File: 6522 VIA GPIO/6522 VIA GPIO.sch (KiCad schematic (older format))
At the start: 11 parts

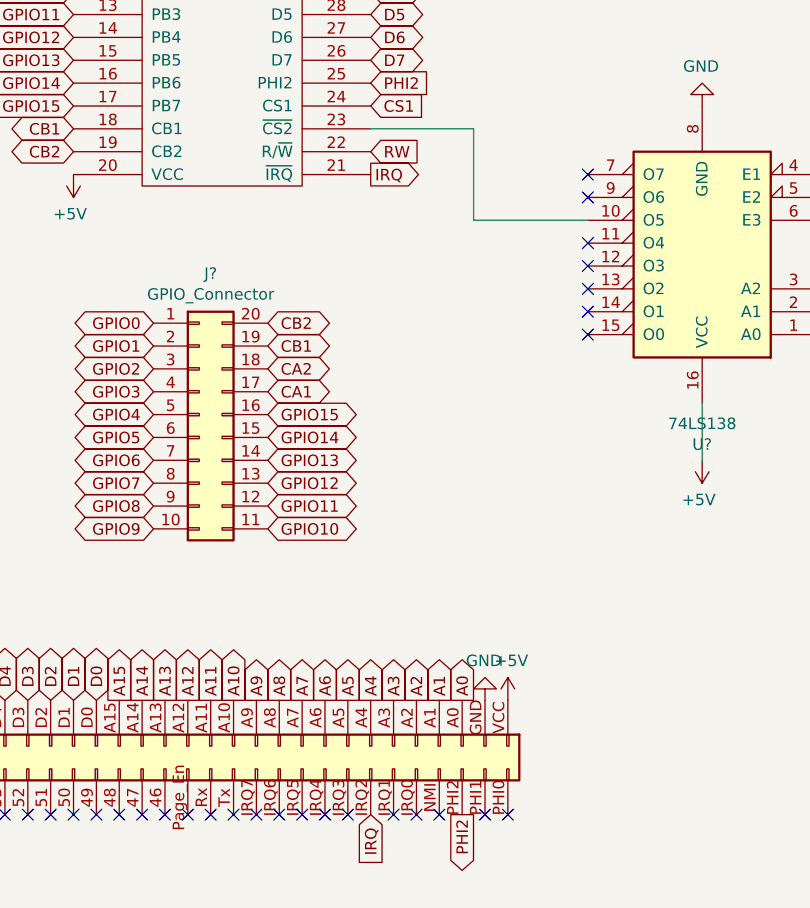
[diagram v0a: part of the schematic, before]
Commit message: Restored SerialIO back to 6521 PIA...
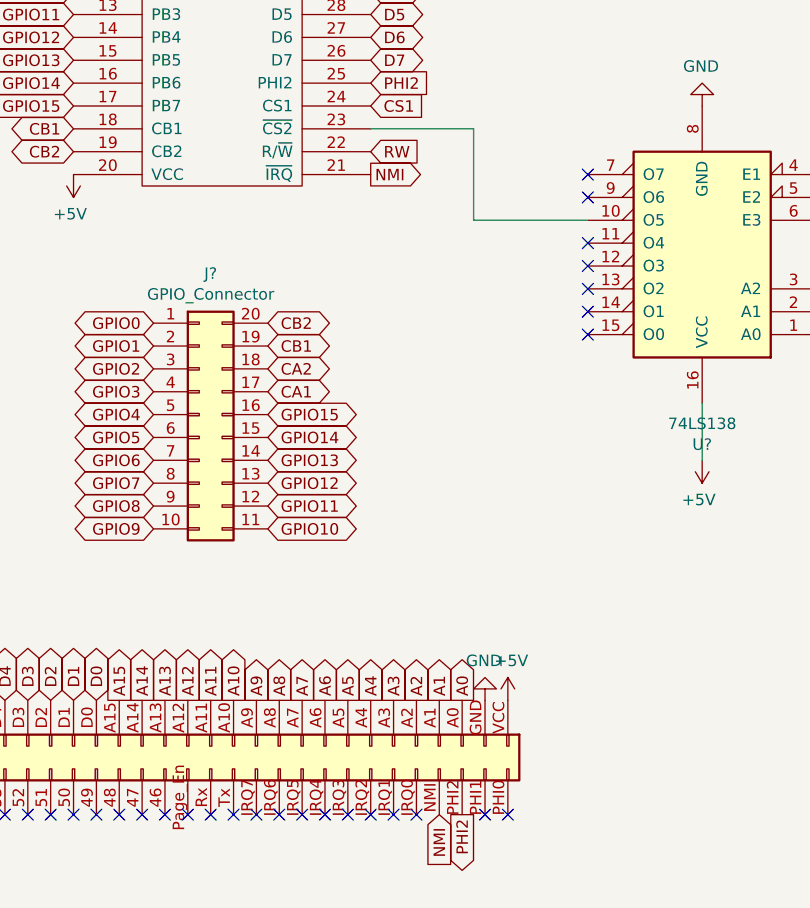
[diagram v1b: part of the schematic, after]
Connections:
- net NMI: now reaches J?.NMI
- net NMI: now also U?.21 (~IRQ)
- net IRQ: no longer names the net of J?.IRQ2
- net IRQ: no longer U?.21 (~IRQ)
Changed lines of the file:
@@
 Text GLabel 4450 3550 2    50   BiDi ~ 0
 D7
-Text GLabel 4450 4050 2    50   Output ~ 0
-IRQ
 Text GLabel 3150 2250 0    50   Output ~ 0
 GPIO0
@@
 Text GLabel 8800 3900 2    50   Input ~ 0
 A9
-NoConn ~ 4750 6850
-Text GLabel 4450 6850 3    50   Input ~ 0
-IRQ
+Text GLabel 4450 4050 2    50   Output ~ 0
+NMI
+Text GLabel 4750 6850 3    50   Input ~ 0
+NMI
+NoConn ~ 4450 6850
 $EndSCHEMATC
